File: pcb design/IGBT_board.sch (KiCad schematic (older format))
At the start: 68 parts, among them J1 4-794627-0, Q1 IGBT, Q10 IGBT, Q11 IGBT, Q12 IGBT, Q2 IGBT, Q3 IGBT, Q4 IGBT, Q5 IGBT, Q6 IGBT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

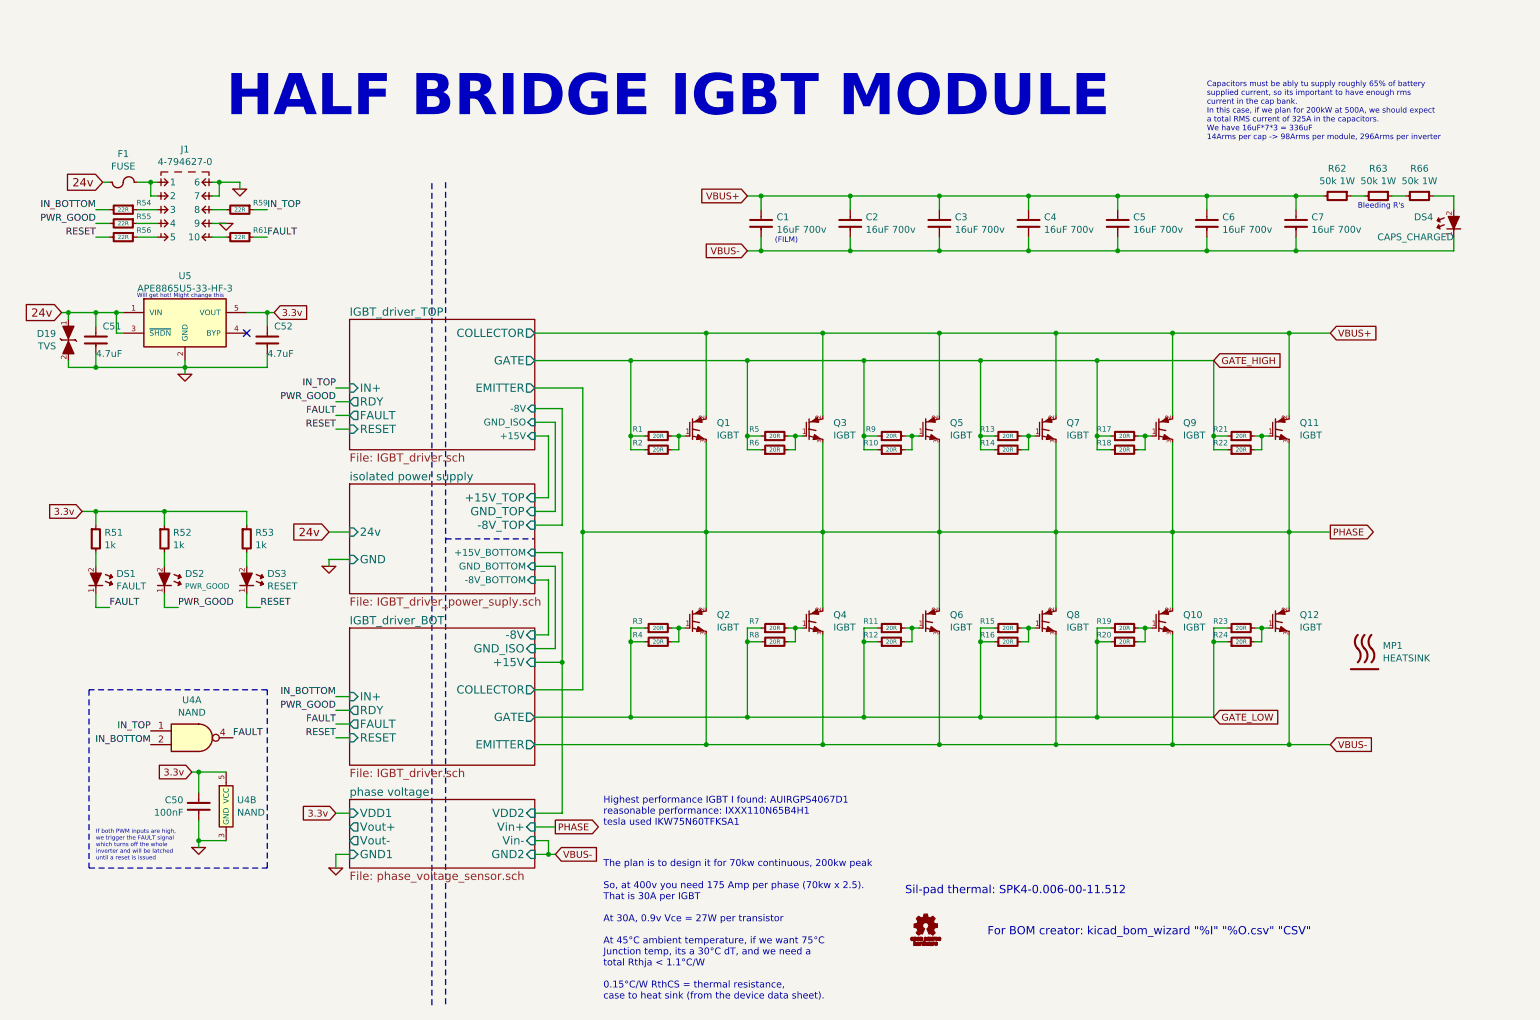
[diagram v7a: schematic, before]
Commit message: Updated gate resistor rating, qty and part#, updated desat blocking diode with much beetter recovery time
Signed-off-by: Marcos Chaparro <mchaparro@paltatech.com>
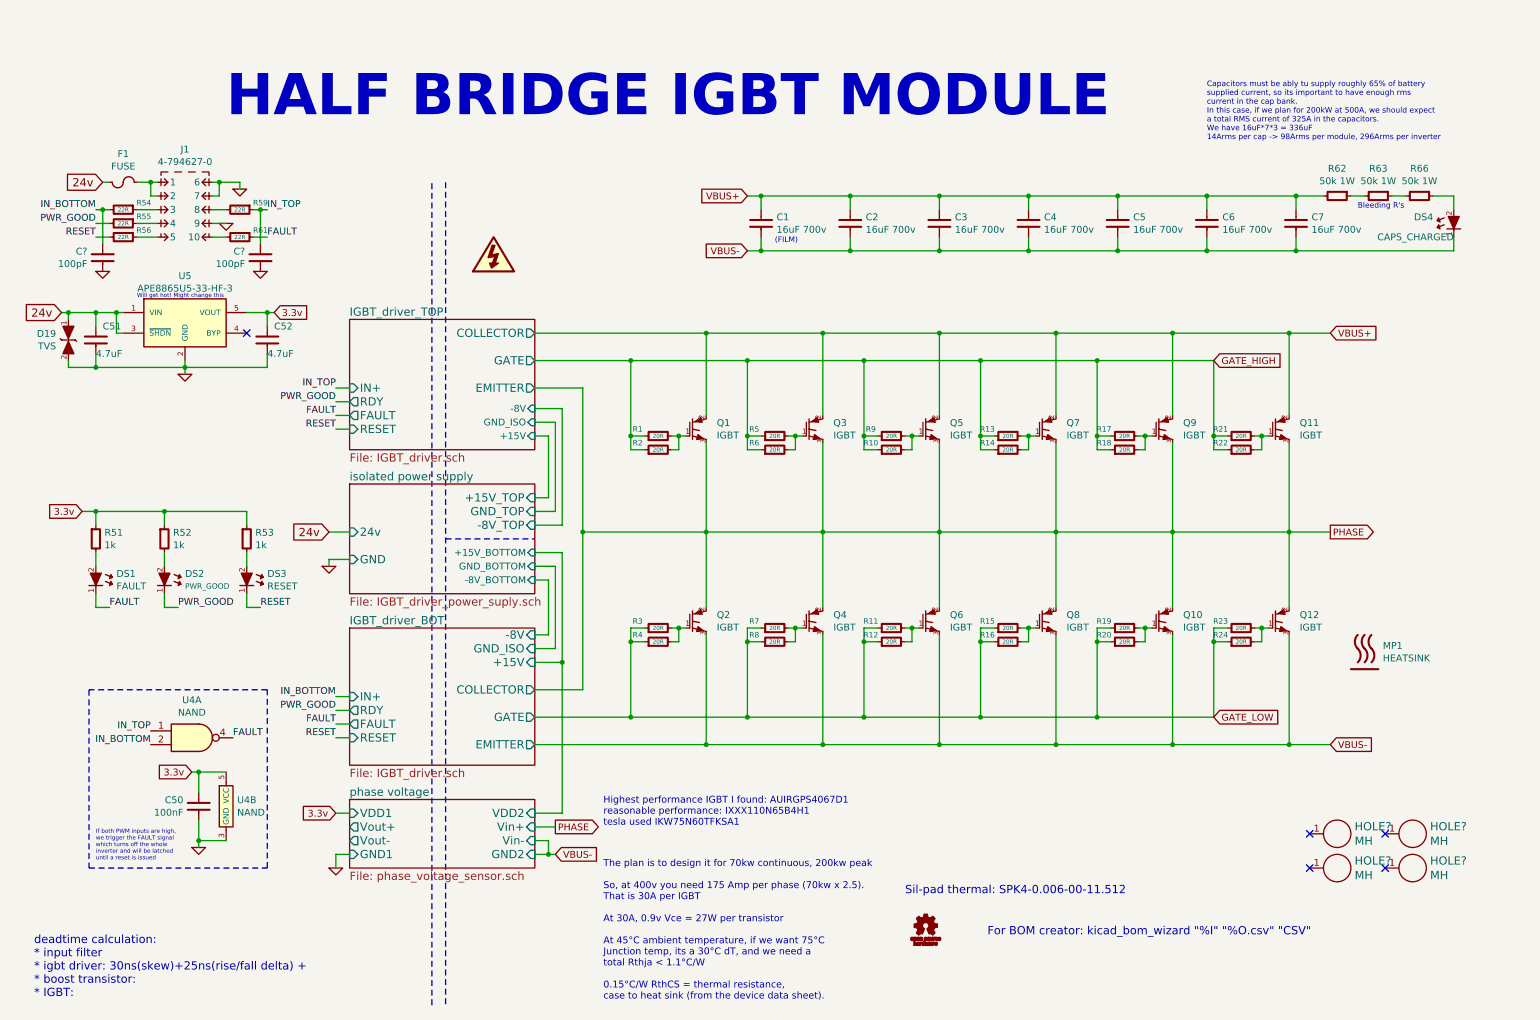
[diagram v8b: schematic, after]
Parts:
- added C? (x2): 100pF, IPC7351-Nominal:CAPC1608X55, symbol C-0603
- added HOLE? (x4): MH, symbol MOUNTING_HOLE
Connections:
- net GND: now also C?.2, C?.2
- net IN_BOTTOM: now also C?.1
- net IN_TOP: now also C?.1
- no-connect marks 1 -> 5
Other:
- note added: "deadtime calculation:\n* input filter\n* igbt driver: 30ns(skew)+25ns(rise/fall delta) + \n* boost transistor:\n* IGBT:"
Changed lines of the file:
@@
 Wire Wire Line
 	2850 6350 2950 6350
+$Comp
+L MOUNTING_HOLE HOLE?
+U 1 1 585C45CA
+P 10150 6500
+F 0 "HOLE?" H 10277 6553 60  0000 L CNN
+F 1 "MH" H 10277 6447 60  0000 L CNN
+F 2 "" H 10150 6500 60  0000 C CNN
+F 3 "" H 10150 6500 60  0000 C CNN
+	1    10150 6500
+	1    0    0    -1
+$EndComp
+NoConn ~ 9950 6500
+$Comp
+L MOUNTING_HOLE HOLE?
+U 1 1 585C56CA
+P 10150 6750
+F 0 "HOLE?" H 10277 6803 60  0000 L CNN
+F 1 "MH" H 10277 6697 60  0000 L CNN
+F 2 "" H 10150 6750 60  0000 C CNN
+F 3 "" H 10150 6750 60  0000 C CNN
+	1    10150 6750
+	1    0    0    -1
+$EndComp
+$Comp
+L MOUNTING_HOLE HOLE?
+U 1 1 585C5DBC
+P 10700 6750
+F 0 "HOLE?" H 10827 6803 60  0000 L CNN
+F 1 "MH" H 10827 6697 60  0000 L CNN
+F 2 "" H 10700 6750 60  0000 C CNN
+F 3 "" H 10700 6750 60  0000 C CNN
+	1    10700 6750
+	1    0    0    -1
+$EndComp
+$Comp
+L HV #SYM?
+U 1 1 585C631E
+P 4000 2300
+F 0 "#SYM?" H 4000 2300 60  0001 C CNN
+F 1 "HV" H 4000 2300 60  0001 C CNN
+F 2 "" H 3900 2200 60  0000 C CNN
+F 3 "" H 4000 2300 60  0000 C CNN
+	1    4000 2300
+	1    0    0    -1
+$EndComp
+$Comp
+L MOUNTING_HOLE HOLE?
+U 1 1 585C7B75
+P 10700 6500
+F 0 "HOLE?" H 10827 6553 60  0000 L CNN
+F 1 "MH" H 10827 6447 60  0000 L CNN
+F 2 "" H 10700 6500 60  0000 C CNN
+F 3 "" H 10700 6500 60  0000 C CNN
+	1    10700 6500
+	1    0    0    -1
+$EndComp
+NoConn ~ 9950 6750
+NoConn ~ 10500 6750
+NoConn ~ 10500 6500
+$Comp
+L C-0603 C?
+U 1 1 585F404D
+P 1150 2300
+F 0 "C?" H 1262 2346 50  0000 L CNN
+F 1 "100pF" H 1262 2255 50  0000 L CNN
+F 2 "IPC7351-Nominal:CAPC1608X55" H 1150 2300 50  0001 C CNN
+F 3 "" H 1140 2275 60  0000 C CNN
+F 4 "CAP MLCC 100pF C0G 50V 5% [0603]" H 1950 2850 60  0001 C CNN "BOM"
+	1    1150 2300
+	-1   0    0    -1
+$EndComp
+$Comp
+L C-0603 C?
+U 1 1 585F49C0
+P 2300 2300
+F 0 "C?" H 2412 2346 50  0000 L CNN
+F 1 "100pF" H 2412 2255 50  0000 L CNN
+F 2 "IPC7351-Nominal:CAPC1608X55" H 2300 2300 50  0001 C CNN
+F 3 "" H 2290 2275 60  0000 C CNN
+F 4 "CAP MLCC 100pF C0G 50V 5% [0603]" H 3100 2850 60  0001 C CNN "BOM"
+	1    2300 2300
+	-1   0    0    -1
+$EndComp
+Wire Wire Line
+	2300 2200 2300 1950
+Connection ~ 2300 1950
+$Comp
+L GND #PWR?
+U 1 1 585F4F4E
+P 2300 2400
+F 0 "#PWR?" H 2300 2400 30  0001 C CNN
+F 1 "GND" H 2300 2330 30  0001 C CNN
+F 2 "" H 2300 2400 60  0000 C CNN
+F 3 "" H 2300 2400 60  0000 C CNN
+	1    2300 2400
+	1    0    0    -1
+$EndComp
+$Comp
+L GND #PWR?
+U 1 1 585F510F
+P 1150 2400
+F 0 "#PWR?" H 1150 2400 30  0001 C CNN
+F 1 "GND" H 1150 2330 30  0001 C CNN
+F 2 "" H 1150 2400 60  0000 C CNN
+F 3 "" H 1150 2400 60  0000 C CNN
+	1    1150 2400
+	1    0    0    -1
+$EndComp
+Wire Wire Line
+	1150 2200 1150 1950
+Connection ~ 1150 1950
+Text Notes 650  7700 0    60   ~ 0
+deadtime calculation:\n* input filter\n* igbt driver: 30ns(skew)+25ns(rise/fall delta) + \n* boost transistor:\n* IGBT:
 $EndSCHEMATC
